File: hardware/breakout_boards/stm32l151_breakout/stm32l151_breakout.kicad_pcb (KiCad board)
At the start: 2 copper layers, 12 parts, among them J1 USB_B_Micro, J2 Conn_01x24_Male, J3 Conn_ARM_JTAG_SWD_10, J4 Conn_01x24_Male, U1 LD1117-3.3, U2 STM32L151C

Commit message: Finish out initial board
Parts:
- added D1: LED, LEDs:LED_0805_HandSoldering, F.Cu at (48.3, 50.8)
- added R1: 40, Resistors_SMD:R_0805_HandSoldering, F.Cu at (54.6, 52.1)
- 0.1uF1: value C -> C1
- 0.1uF2: value C -> C2
- 0.1uF3: value C -> C3
- 0.1uF4: value C -> C4
- 0.1uF5: value C -> C5
- 10uF1: value C -> C6
- moved 0.1uF5 52.2 mm to (43.2, 30.5)
- moved J4 49.9 mm to (66.0, 24.1)
- moved 10uF1 48.9 mm to (41.9, 22.9)
- moved 0.1uF1 43.7 mm to (41.9, 26.7)
- moved 0.1uF3 42.4 mm to (53.3, 47.0), turned to 180 degrees
- moved 0.1uF4 34.2 mm to (57.1, 29.2)
- moved 0.1uF2 28.5 mm to (43.2, 41.9), turned to 180 degrees
- moved U2 25.6 mm to (50.8, 36.8)
- moved J3 21.7 mm to (47.0, 25.4)
- moved U1 15.5 mm to (57.1, 58.4), turned to 270 degrees
- moved J1 14.2 mm to (43.2, 59.7), turned to 0 degrees
- moved J2 13.9 mm to (33.0, 24.1)
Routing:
- net /+3.3V: track 0.00 -> 109.8 mm
- net GND: track 0.00 -> 66.3 mm, vias 0 -> 9
- net Net-(J4-Pad10): track 0.00 -> 61.8 mm, vias 0 -> 3
- net /JTRST: track 0.00 -> 54.3 mm, vias 0 -> 4
- net /VLCD: track 0.00 -> 47.8 mm, vias 0 -> 2
- net /JTDO: track 0.00 -> 42.6 mm, vias 0 -> 6
- net /JTMS: track 0.00 -> 42.5 mm, vias 0 -> 2
- net Net-(J4-Pad7): track 0.00 -> 41.4 mm, vias 0 -> 3
- net Net-(J4-Pad8): track 0.00 -> 39.1 mm
- net Net-(J4-Pad6): track 0.00 -> 38.7 mm, vias 0 -> 2
- net /JTCK: track 0.00 -> 37.0 mm, vias 0 -> 4
- net /JTDI: track 0.00 -> 36.3 mm, vias 0 -> 2
- net Net-(J2-Pad18): track 0.00 -> 28.5 mm
- net Net-(J1-Pad1): track 0.00 -> 27.4 mm, vias 0 -> 2
- net Net-(J2-Pad10): track 0.00 -> 26.9 mm
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- added copper zone on B.Cu, net GND
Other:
- net class Default: clearance 0.2 -> 0.1524; trace_width 0.25 -> 0.1524; via_dia 0.8 -> 0.6858; via_drill 0.4 -> 0.3302
- rule trace_clearance: 0.2 -> 0.1524
- rule trace_min: 0.2 -> 0.1524
- rule via_min_drill: 0.3 -> 0.3302
- rule via_min_size: 0.4 -> 0.6858

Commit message: Add logo and such
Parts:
- added REF***: OSHW-Logo2_7.3x6mm_SilkScreen, Symbols:OSHW-Logo2_7.3x6mm_SilkScreen, F.Cu at (67.3, 61.0)
- moved 0.1uF3 1.27 mm to (53.3, 45.7)
- moved R1 1.27 mm to (54.6, 50.8)
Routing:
- net /VDD_1: track 6.24 -> 5.04 mm
- net GND: track 66.3 -> 65.6 mm
- net Net-(D1-Pad1): track 7.78 -> 7.25 mm
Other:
- board text added: "Blake Smith"
- board text added: "STM32L151C Breakout Board Rev. A"

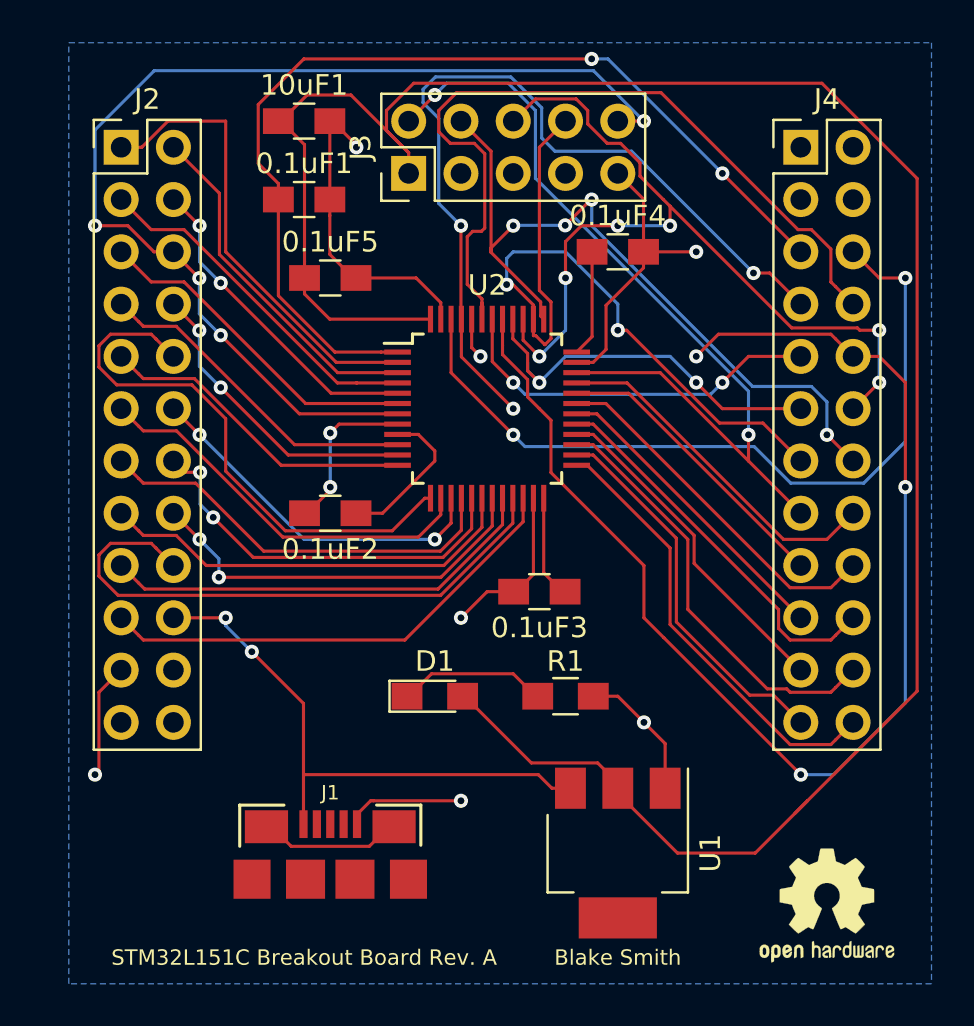
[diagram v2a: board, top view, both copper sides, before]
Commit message: Correct board outline
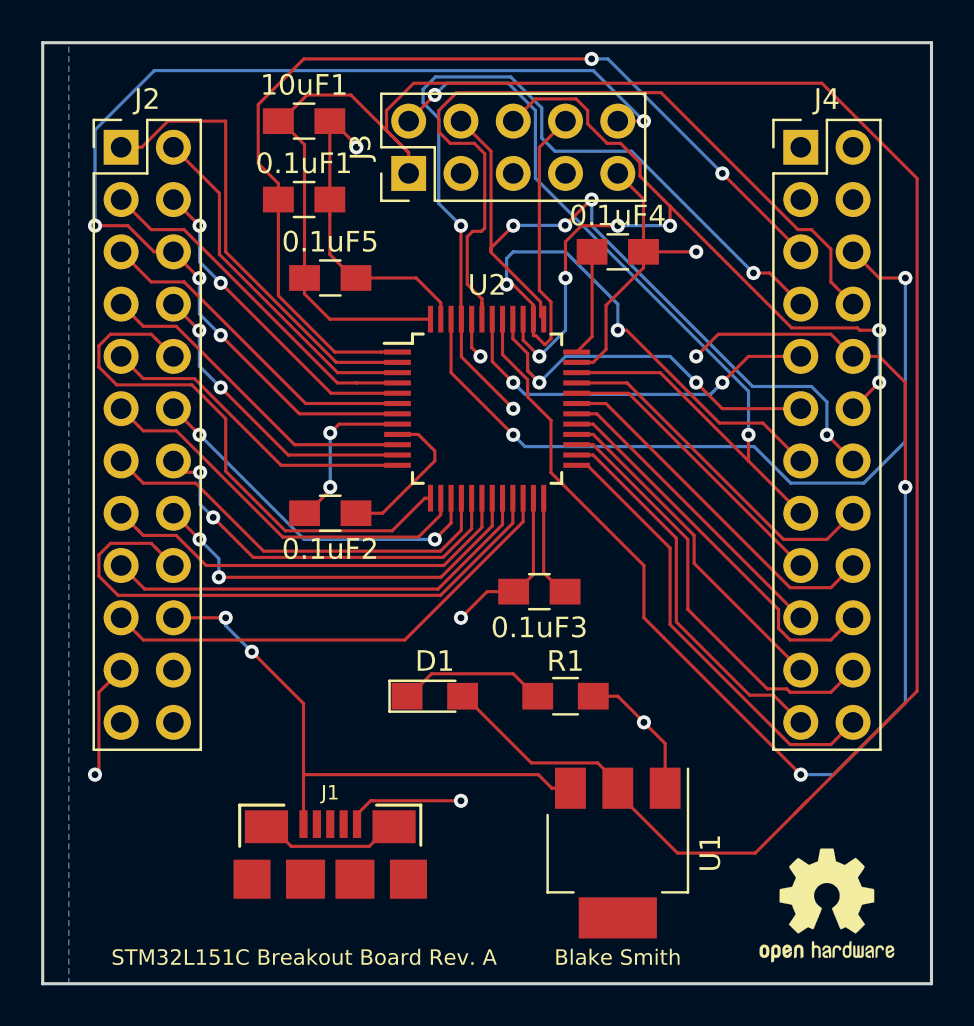
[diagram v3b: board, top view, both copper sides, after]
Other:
- board outline added: 43.2 x 45.7 mm
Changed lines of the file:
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@@
   (general
     (thickness 1.6)
-    (drawings 2)
+    (drawings 6)
     (tracks 503)
     (zones 0)
@@
       (effects (font (size 1 1) (thickness 0.15)))
     )
-    (fp_text value Conn_01x24_Male (at 1.27 30.27) (layer F.Fab)
+    (fp_text value Conn_01x24_Male (at 5.08 30.48) (layer F.Fab)
       (effects (font (size 1 1) (thickness 0.15)))
     )
@@
       (effects (font (size 1 1) (thickness 0.15)))
     )
-    (fp_text value Conn_ARM_JTAG_SWD_10 (at 1.27 12.49 90) (layer F.Fab)
+    (fp_text value Conn_ARM_JTAG_SWD_10 (at -2.54 13.97 90) (layer F.Fab)
       (effects (font (size 1 1) (thickness 0.15)))
     )
@@
       (effects (font (size 1 1) (thickness 0.15)))
     )
-    (fp_text value Conn_01x24_Male (at 1.27 30.27) (layer F.Fab)
+    (fp_text value Conn_01x24_Male (at 0 31.75) (layer F.Fab)
       (effects (font (size 1 1) (thickness 0.15)))
     )
@@
     )
   )
+  (gr_line (start 72.39 19.05) (end 29.21 19.05) (layer Edge.Cuts) (width 0.15))
+  (gr_line (start 72.39 64.77) (end 72.39 19.05) (layer Edge.Cuts) (width 0.15))
+  (gr_line (start 29.21 64.77) (end 72.39 64.77) (layer Edge.Cuts) (width 0.15))
+  (gr_line (start 29.21 19.05) (end 29.21 64.77) (layer Edge.Cuts) (width 0.15))
   (gr_text "Blake Smith\n" (at 57.15 63.5) (layer F.SilkS)
     (effects (font (size 0.75 0.75) (thickness 0.1875)))
@@
       )
     )
-  )
-  (zone (net 0) (net_name "") (layer Edge.Cuts) (hatch edge 0.508)
-    (connect_pads (clearance 0.508))
-    (min_thickness 0.254)
-    (fill yes (arc_segments 16) (thermal_gap 0.508) (thermal_bridge_width 0.508))
-    (polygon
-      (pts
-        (xy 30.48 19.05) (xy 30.48 64.77) (xy 72.39 64.77) (xy 72.39 19.05)
-      )
-    )

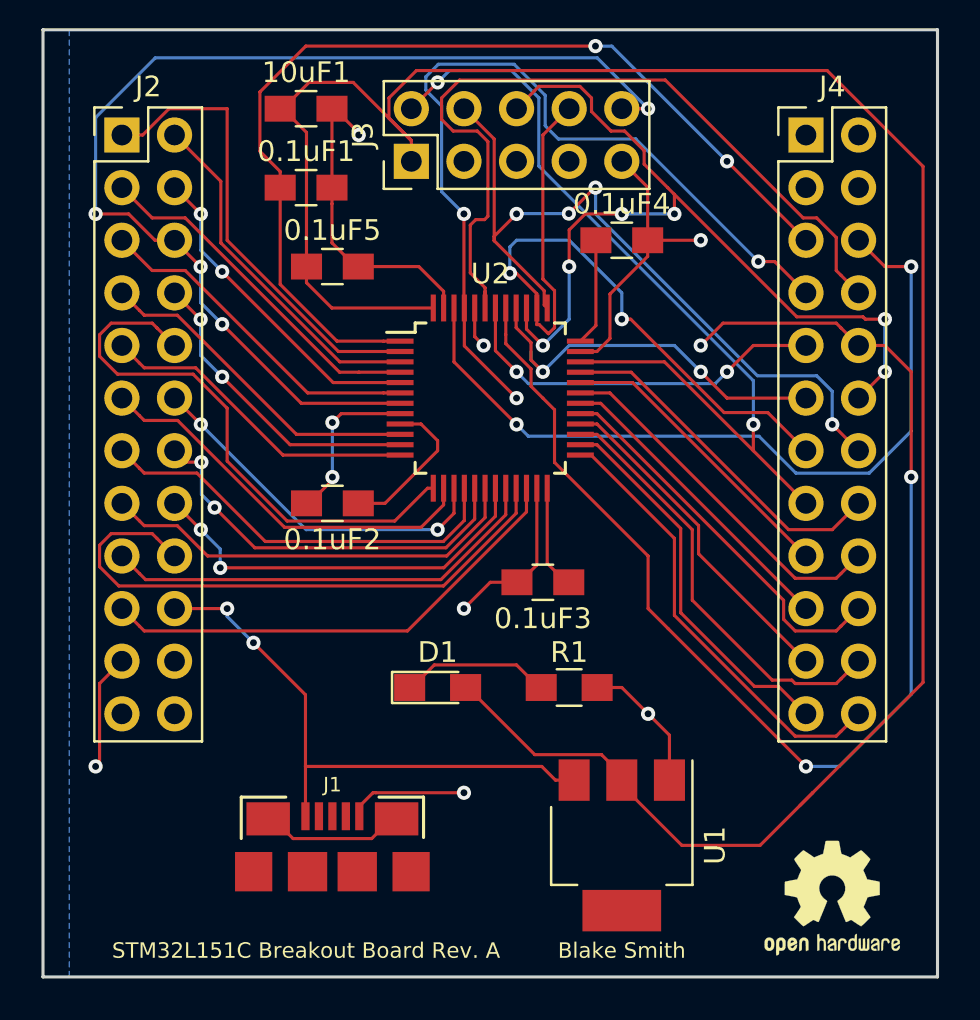
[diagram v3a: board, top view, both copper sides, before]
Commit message: Add breakout board pin labels
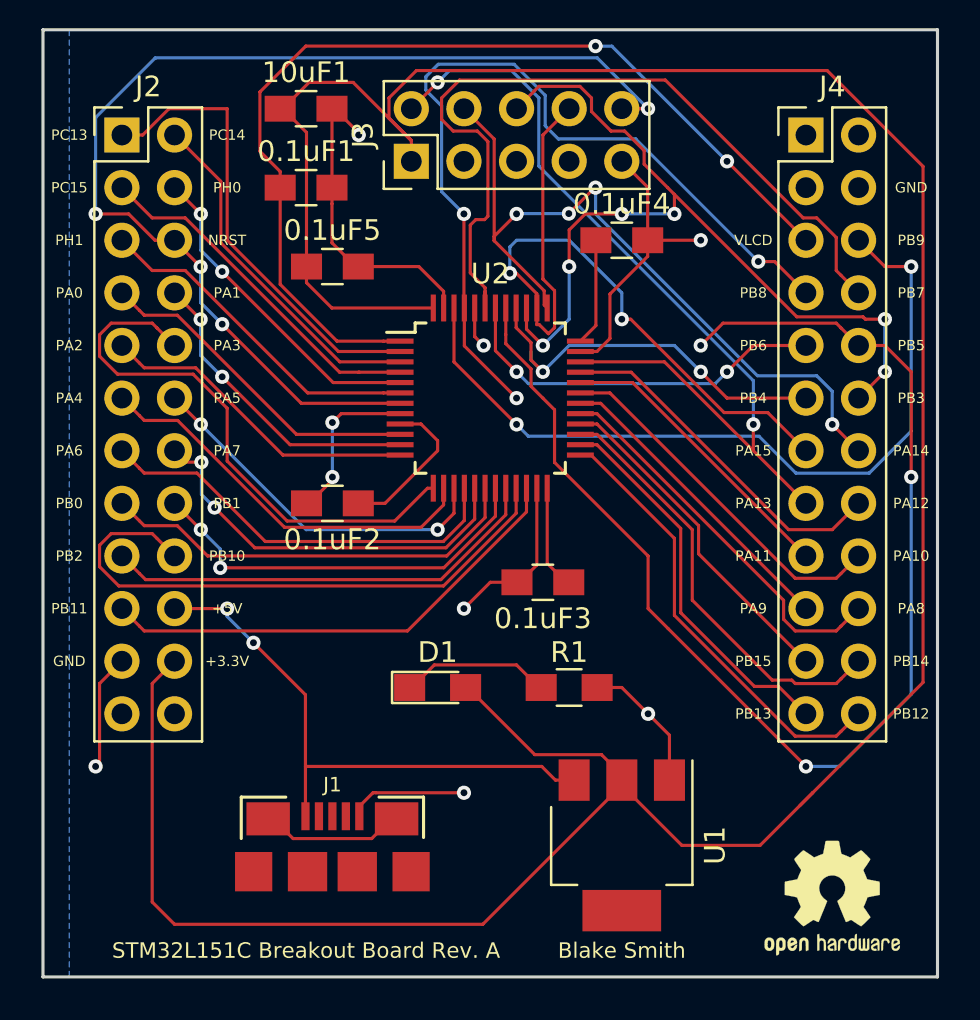
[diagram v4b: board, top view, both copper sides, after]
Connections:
- J2 pad 22: Net-(J2-Pad22) -> /+3.3V
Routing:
- net /+3.3V: track 109.7 -> 147.7 mm
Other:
- board text added: "+3.3V"
- board text added: "+5V"
- board text added: "GND"
- board text added: "NRST"
- board text added: "PA0"
- board text added: "PA1"
- board text added: "PA10"
- board text added: "PA11"
- board text added: "PA12"
- board text added: "PA13"
- board text added: "PA14"
- board text added: "PA15"
- board text added: "PA2"
- board text added: "PA3"
- board text added: "PA4"
- board text added: "PA5"
- board text added: "PA6"
- board text added: "PA7"
- board text added: "PA8"
- board text added: "PA9"
- board text added: "PB0"
- board text added: "PB1"
- board text added: "PB10"
- board text added: "PB11"
- board text added: "PB12"
- board text added: "PB13"
- board text added: "PB14"
- board text added: "PB15"
- board text added: "PB2"
- board text added: "PB3"
- board text added: "PB4"
- board text added: "PB5"
- board text added: "PB6"
- board text added: "PB7"
- board text added: "PB8"
- board text added: "PB9"
- board text added: "PC13"
- board text added: "PC14"
- board text added: "PC15"
- board text added: "PH0"
- board text added: "PH1"
- board text added: "VLCD"

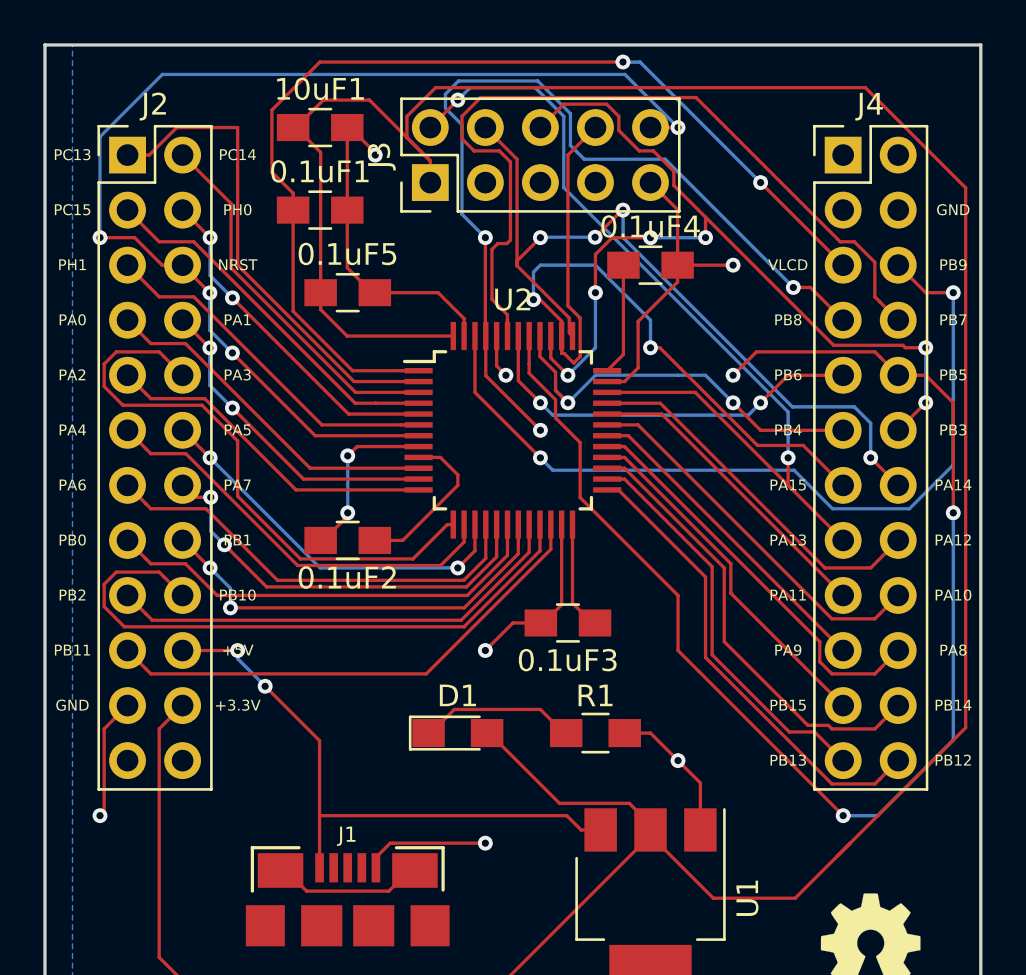
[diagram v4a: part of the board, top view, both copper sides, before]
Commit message: Update stm32l breakout board to use a 1.27mm jtag connector
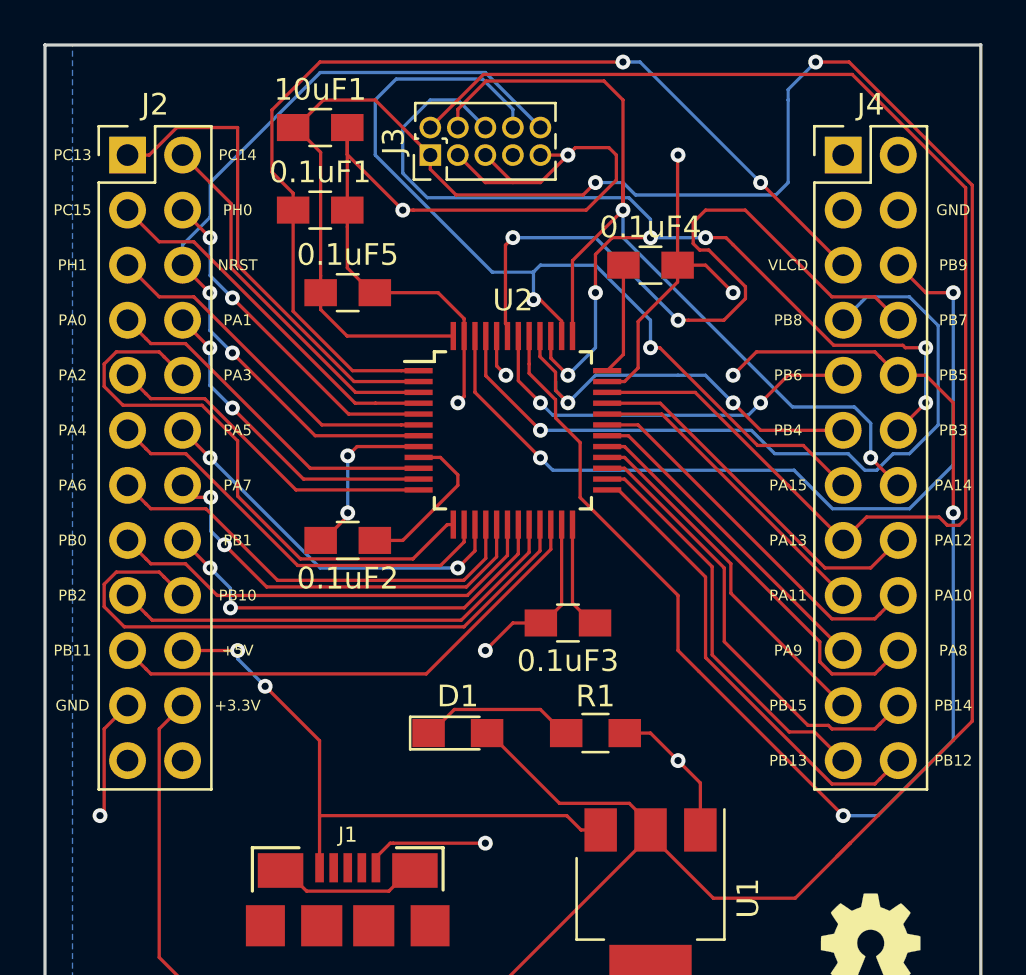
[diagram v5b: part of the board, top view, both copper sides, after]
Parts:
- J3: footprint Pin_Headers:Pin_Header_Straight_2x05_Pitch2.54mm -> Pin_Headers:Pin_Header_Straight_2x05_Pitch1.27mm
- R1: value 40 -> 300
- moved J3 1.27 mm to (47.0, 24.1)
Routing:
- net GND: track 65.6 -> 96.5 mm, vias 9 -> 12
- net /JTMS: track 42.5 -> 63.3 mm, vias 2 -> 0
- net /JTRST: track 54.3 -> 37.9 mm, vias 4 -> 2
- net /JTDO: track 42.6 -> 50.4 mm
- net /JTDI: track 36.3 -> 43.3 mm
- net Net-(J4-Pad7): track 41.4 -> 35.4 mm, vias 3 -> 1
- net Net-(J4-Pad8): track 39.1 -> 34.0 mm, vias 0 -> 2
- net /JTCK: track 37.0 -> 42.1 mm, vias 4 -> 2
- net /+3.3V: track 147.7 -> 150.1 mm, vias 0 -> 2

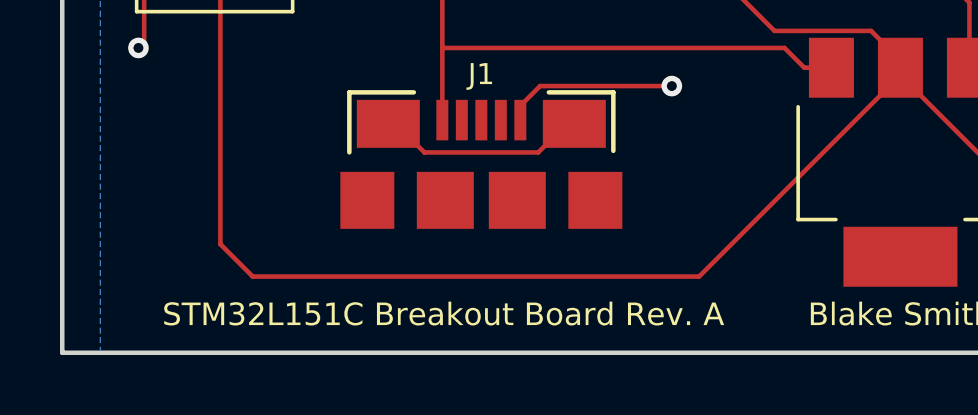
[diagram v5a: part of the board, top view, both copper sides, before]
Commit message: Update title to be Rev. B
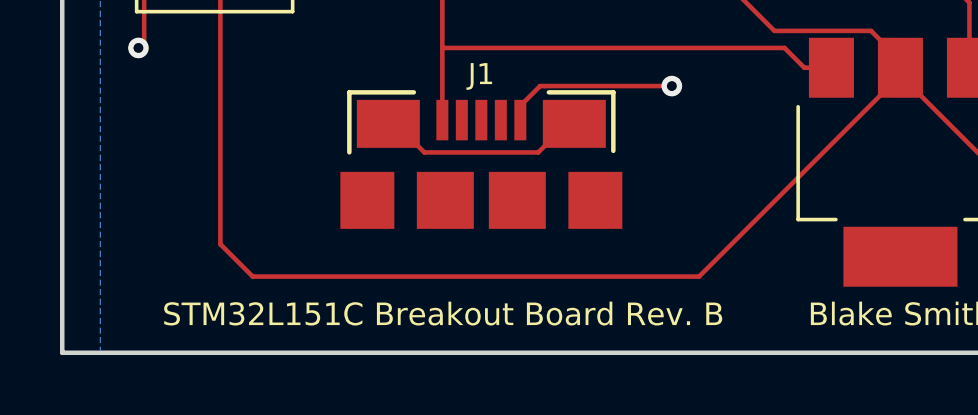
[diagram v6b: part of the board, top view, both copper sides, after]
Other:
- board text added: "STM32L151C Breakout Board Rev. B"
- board text removed: "STM32L151C Breakout Board Rev. A"
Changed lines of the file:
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@@
     (effects (font (size 0.75 0.75) (thickness 0.1875)))
   )
-  (gr_text "STM32L151C Breakout Board Rev. A" (at 41.91 63.5) (layer F.SilkS)
+  (gr_text "STM32L151C Breakout Board Rev. B" (at 41.91 63.5) (layer F.SilkS)
     (effects (font (size 0.75 0.75) (thickness 0.1875)))
   )
